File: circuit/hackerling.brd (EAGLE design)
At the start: 82.5 x 67.4 mm, 45 parts, among them IC1 MCP23017SP, IC2 MCP2300X/P, IC3 MIC5219BM5, SW2 SWITCH_B13EH, U1 MMA8452Q, U2 LCD_16X2, U3 ARDUINOR3-BPLACE, U5 PCA9306, U7 POT

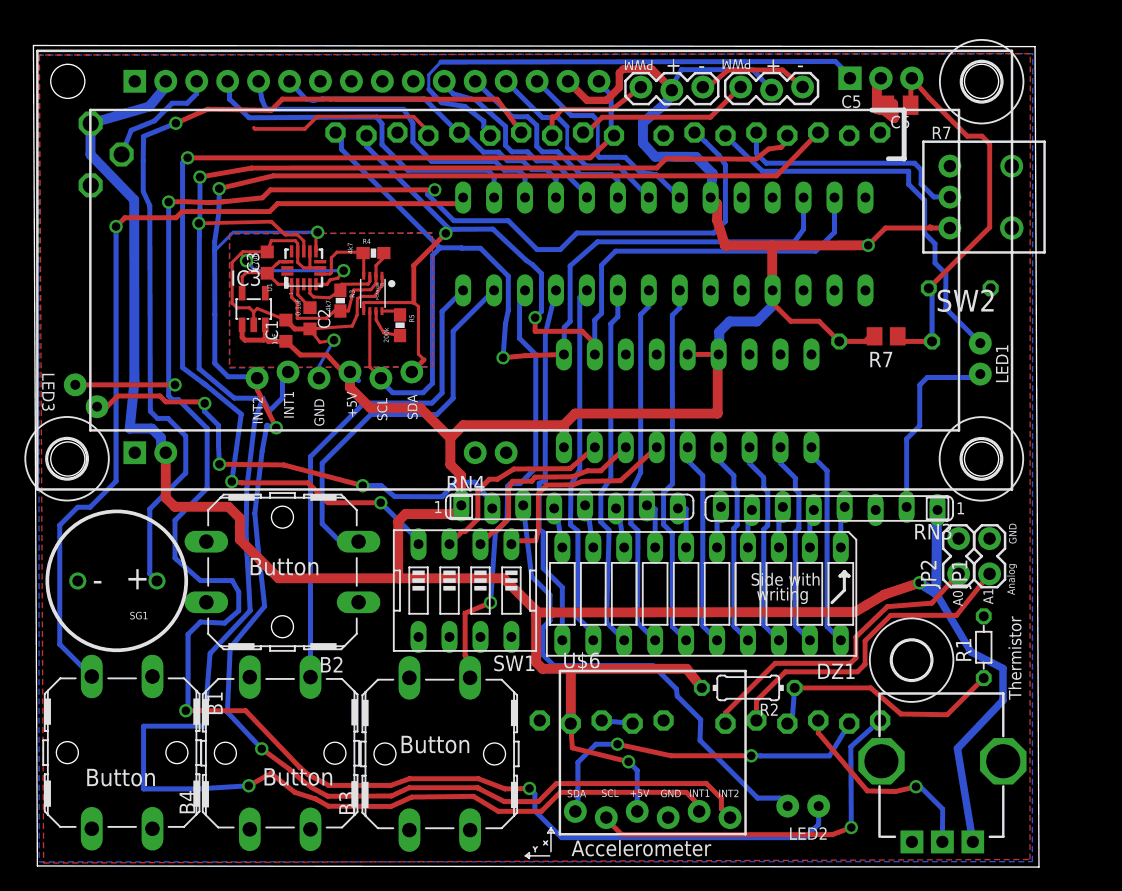
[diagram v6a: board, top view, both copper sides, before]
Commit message: resubmitting circuit version 1.1 was held for drill overlap modified board slightly, mostly in soldermask to improve readability the ir reciever shifted, and moved a few vias.
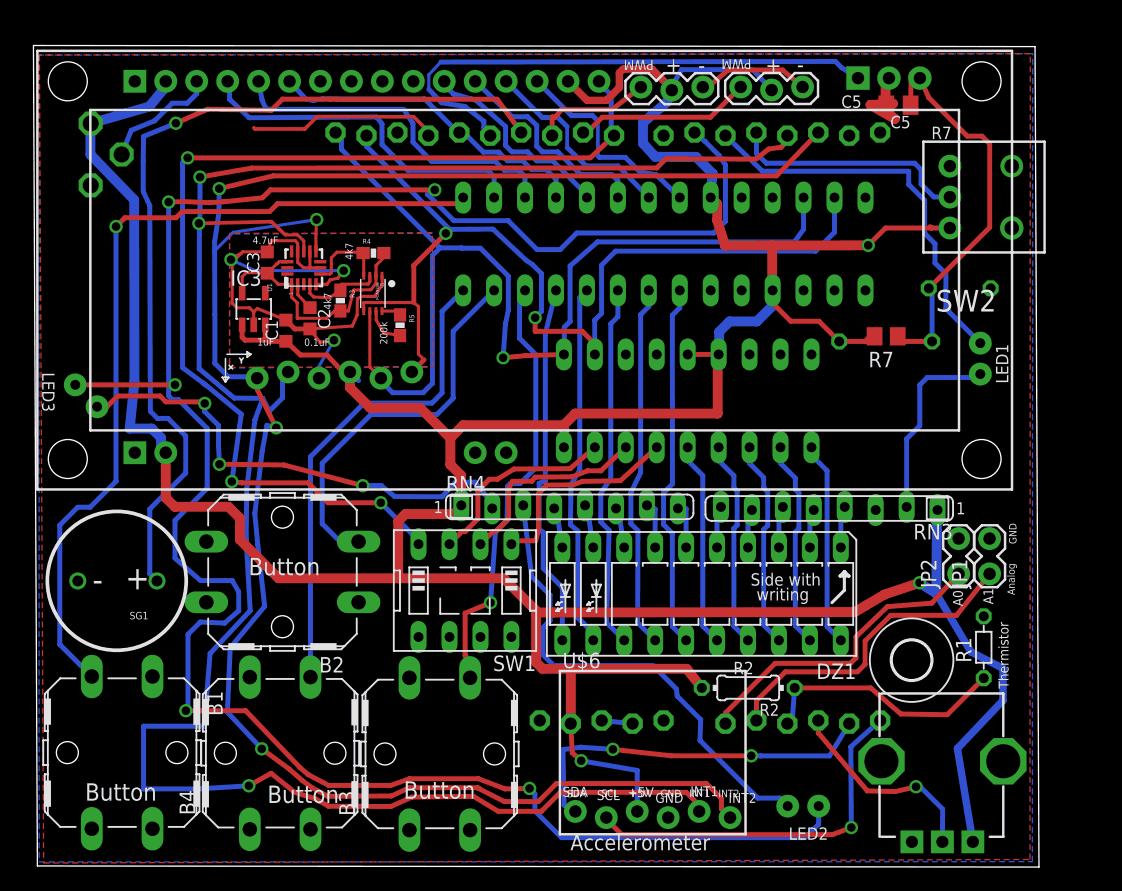
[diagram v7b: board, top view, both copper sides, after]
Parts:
- removed H1, H3, H4: MOUNTHOLE'3.2, hackerscouts:HOLE_3.2
- moved IR1 0.66 mm to (70.0, 64.7)
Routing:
- net GND: track 84.4 -> 88.3 mm
- net SDA1: track 28.6 -> 30.7 mm
- net A_INT2: track 157.3 -> 158.2 mm
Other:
- board text added: "1.1"
- board text added: "1/4 inch away"
- board text added: "18"
- board text added: "18,19,20:"
- board text added: "19"
- board text added: "21"
- board text added: "Bargraph"
- board text added: "For steps"
- board text added: "Install"
- board text added: "Install Pot."
- board text added: "Other"
- board text added: "R2"
- board text added: "See"
- board text added: "Side"
- board text added: "Solder LEDs"
- board text added: "This Circuit is Open Source!"
- board text added: "as last step"
- board text added: "circuit.hacker-scouts.org"
- board text added: "from board"
- board text added: "switch"
- board text removed: "1.0"
- board text removed: "Install switch"
- board text removed: "Leave .25" out"
- board text removed: "Step 18:"
- board text removed: "Step 19:"
- board text removed: "Step 21:"

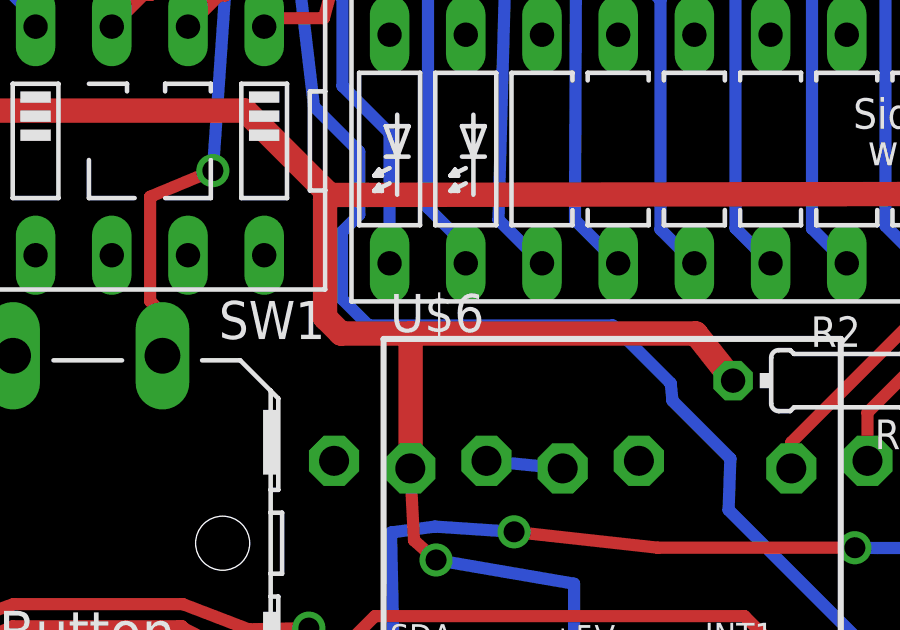
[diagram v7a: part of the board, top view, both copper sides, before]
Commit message: documenting updated values in eagle files filled out BOM writing installation instructions
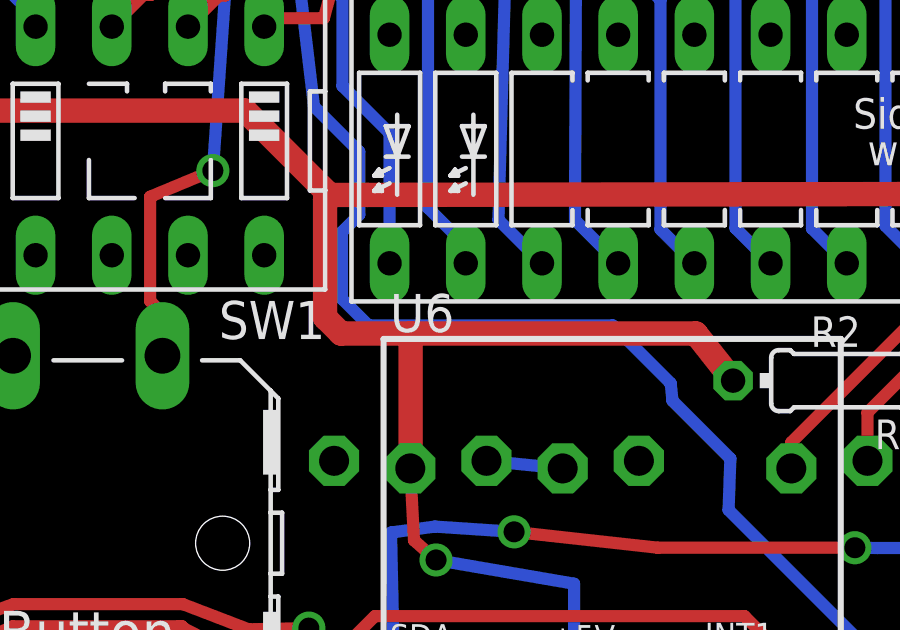
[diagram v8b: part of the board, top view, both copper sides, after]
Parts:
- C5: value (none) -> 10uF
- renumbered U$3 to U4, U$6 to U6, U$8 to U8
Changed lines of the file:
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@@
 <setting verticaltext="up"/>
 </settings>
-<grid distance="0.005842" unitdist="mm" unit="mm" style="lines" multiple="100" display="yes" altdistance="0.025" altunitdist="inch" altunit="inch"/>
+<grid distance="0.005" unitdist="mm" unit="mm" style="lines" multiple="100" display="yes" altdistance="0.025" altunitdist="inch" altunit="inch"/>
 <layers>
 <layer number="1" name="Top" color="4" fill="1" visible="yes" active="yes"/>
@@
 <element name="IC2" library="adafruit" package="DIL18" value="MCP2300X/P" x="53.43" y="38.22" rot="MR180"/>
 <element name="IR1" library="adafruit" package="PNA460XM" value="PNA460XM" x="69.95" y="64.715" rot="MR180"/>
-<element name="U$3" library="hackerscouts" package="ACCELEROMETER" value="ACCELEROMETER" x="24.44" y="45.42" smashed="yes" rot="MR0">
+<element name="U4" library="hackerscouts" package="ACCELEROMETER" value="ACCELEROMETER" x="24.44" y="45.42" smashed="yes" rot="MR0">
 <attribute name="NAME" x="31.8462" y="52.3488" size="1.27" layer="26" ratio="10" rot="MR0"/>
 <attribute name="VALUE" x="16.115" y="52.56" size="1.27" layer="28" rot="MR270"/>
@@
 <element name="U5" library="hackerscouts" package="VSSOP-8" value="PCA9306" x="27.59" y="47.04" rot="R180"/>
 <element name="R5" library="SparkFun" package="0603-RES" value="200K" x="29.82" y="44.43" rot="R270"/>
-<element name="U$6" library="hackerscouts" package="ACCELEROMETER" value="ACCELEROMETER" x="50.56" y="9.35" smashed="yes">
+<element name="U6" library="hackerscouts" package="ACCELEROMETER" value="ACCELEROMETER" x="50.56" y="9.35" smashed="yes">
 <attribute name="NAME" x="43.1538" y="16.2788" size="1.27" layer="25" ratio="10"/>
 <attribute name="VALUE" x="42.94" y="1.095" size="1.27" layer="27"/>
@@
 <element name="B4" library="hackerscouts" package="SWITCH_B3F-4000" value="" x="19.98" y="9.3" rot="R90"/>
 <element name="SW2" library="hackerscouts" package="SWITCH_B13EH" value="SWITCH_B13EH" x="74.95" y="54.95" rot="R180"/>
-<element name="U$8" library="hackerscouts" package="SML_POT" value="SML_POT" x="4.43" y="58.45" rot="MR270"/>
+<element name="U8" library="hackerscouts" package="SML_POT" value="SML_POT" x="4.43" y="58.45" rot="MR270"/>
 <element name="C4" library="rcl" package="C050-050X075" value="10uF" x="75.76" y="47.46" rot="MR180"/>
 <element name="R6" library="resistor" package="0204/7" value="47" x="69.68" y="43.1" rot="MR0"/>
 <element name="R7" library="rcl" package="R0805" value="" x="69.72" y="43.52" rot="R180"/>
-<element name="C5" library="resistor" package="C0805K" value="" x="70.73" y="62.49" rot="R180"/>
+<element name="C5" library="resistor" package="C0805K" value="10uF" x="70.73" y="62.49" rot="R180"/>
 <element name="JP1" library="SparkFun" package="1X02_LOCK" value="" x="78.21" y="24.2" rot="R90"/>
 <element name="JP2" library="SparkFun" package="1X02_LOCK" value="" x="75.67" y="24.2" rot="R90"/>
@@
 <contactref element="SERVO2" pad="3"/>
 <contactref element="SERVO1" pad="3"/>
-<contactref element="U$3" pad="4"/>
+<contactref element="U4" pad="4"/>
 <contactref element="IC3" pad="2"/>
 <contactref element="C2" pad="2"/>
@@
 <contactref element="U5" pad="P$1"/>
 <contactref element="U7" pad="P$1"/>
-<contactref element="U$6" pad="4"/>
+<contactref element="U6" pad="4"/>
 <wire x1="46.37" y1="11.987" x2="48.91" y2="11.733" width="0.4064" layer="16"/>
 <wire x1="57.86" y1="55.25" x2="57.86" y2="54.91" width="0.4064" layer="16"/>
@@
 <contactref element="SW2" pad="3"/>
 <contactref element="U2" pad="1"/>
-<contactref element="U$8" pad="E"/>
+<contactref element="U8" pad="E"/>
 <contactref element="SW1" pad="5"/>
 <contactref element="IC1" pad="15"/>
@@
 <contactref element="IC2" pad="18"/>
 <contactref element="IC1" pad="9"/>
-<contactref element="U$3" pad="3"/>
+<contactref element="U4" pad="3"/>
 <contactref element="SERVO1" pad="2"/>
 <contactref element="SERVO2" pad="2"/>
@@
 <contactref element="C1" pad="1"/>
 <contactref element="U7" pad="P$3"/>
-<contactref element="U$6" pad="3"/>
+<contactref element="U6" pad="3"/>
 <via x="44.689228125" y="8.6817875" extent="1-16" drill="0.7"/>
 <wire x1="44.689228125" y1="8.6817875" x2="43.95415625" y2="9.336903125" width="0.4064" layer="1"/>
@@
 <wire x1="8" y1="54.72" x2="8.02" y2="39.79" width="0.8128" layer="16"/>
 <wire x1="8.02" y1="39.79" x2="7.63" y2="35.95" width="0.8128" layer="16"/>
-<contactref element="U$8" pad="A"/>
+<contactref element="U8" pad="A"/>
 <wire x1="10.59" y1="64.01" x2="9.24" y2="62.38" width="0.8128" layer="16"/>
 <wire x1="9.24" y1="62.38" x2="4.43" y2="60.99" width="0.8128" layer="16"/>
@@
 <contactref element="IC2" pad="1"/>
 <contactref element="U5" pad="P$6"/>
-<contactref element="U$3" pad="2"/>
+<contactref element="U4" pad="2"/>
 <wire x1="24.526" y1="60.247" x2="25.01" y2="59.636" width="0.4064" layer="16"/>
 <wire x1="25.01" y1="59.636" x2="25.01" y2="58.87" width="0.4064" layer="16"/>
@@
 <contactref element="IC2" pad="2"/>
 <contactref element="U5" pad="P$5"/>
-<contactref element="U$3" pad="1"/>
+<contactref element="U4" pad="1"/>
 <wire x1="30.79" y1="40.594" x2="31.793" y2="41.597" width="0.4064" layer="1"/>
 <wire x1="65.48" y1="54.91" x2="65.48" y2="52.06" width="0.4064" layer="16"/>
@@
 </signal>
 <signal name="A_INT2">
-<contactref element="U$3" pad="6"/>
+<contactref element="U4" pad="6"/>
 <contactref element="U3" pad="D2"/>
 <contactref element="U1" pad="9"/>
-<contactref element="U$6" pad="6"/>
+<contactref element="U6" pad="6"/>
 <wire x1="64.15" y1="60.247" x2="60.72" y2="56.69" width="0.4064" layer="1"/>
 <wire x1="60.72" y1="56.69" x2="19.4" y2="56.69" width="0.4064" layer="1"/>
@@
 </signal>
 <signal name="A_INT1">
-<contactref element="U$3" pad="5"/>
+<contactref element="U4" pad="5"/>
 <contactref element="U3" pad="D3"/>
 <contactref element="U1" pad="11"/>
-<contactref element="U$6" pad="5"/>
+<contactref element="U6" pad="5"/>
 <wire x1="61.61" y1="59.993" x2="61.61" y2="59.55" width="0.4064" layer="1"/>
 <wire x1="61.61" y1="59.55" x2="61.1" y2="59.04" width="0.4064" layer="1"/>
@@
 <signal name="SCL1">
 <contactref element="U3" pad="A5"/>
-<contactref element="U$6" pad="2"/>
+<contactref element="U6" pad="2"/>
 <wire x1="69.23" y1="11.987" x2="66.822" y2="9.833" width="0.4064" layer="16"/>
 <wire x1="66.822" y1="9.833" x2="66.862" y2="3.203" width="0.4064" layer="16"/>
@@
 <signal name="SDA1">
 <contactref element="U3" pad="A4"/>
-<contactref element="U$6" pad="1"/>
+<contactref element="U6" pad="1"/>
 <wire x1="66.69" y1="11.733" x2="65.07" y2="9.08" width="0.4064" layer="16"/>
 <wire x1="65.07" y1="9.08" x2="59.4" y2="9.08" width="0.4064" layer="16"/>
@@
 <signal name="N$13">
 <contactref element="U2" pad="3"/>
-<contactref element="U$8" pad="S"/>
+<contactref element="U8" pad="S"/>
 <wire x1="13.13" y1="64.45" x2="13.13" y2="63.43" width="0.4064" layer="16"/>
 <wire x1="13.13" y1="63.43" x2="12.35" y2="62.65" width="0.4064" layer="16"/>
